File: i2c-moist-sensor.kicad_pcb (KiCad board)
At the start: 4 copper layers, 18 x 149 mm, 25 parts, among them IC1 ATTINY441-SSU, P1 CONN_02X03, X1 16MHz

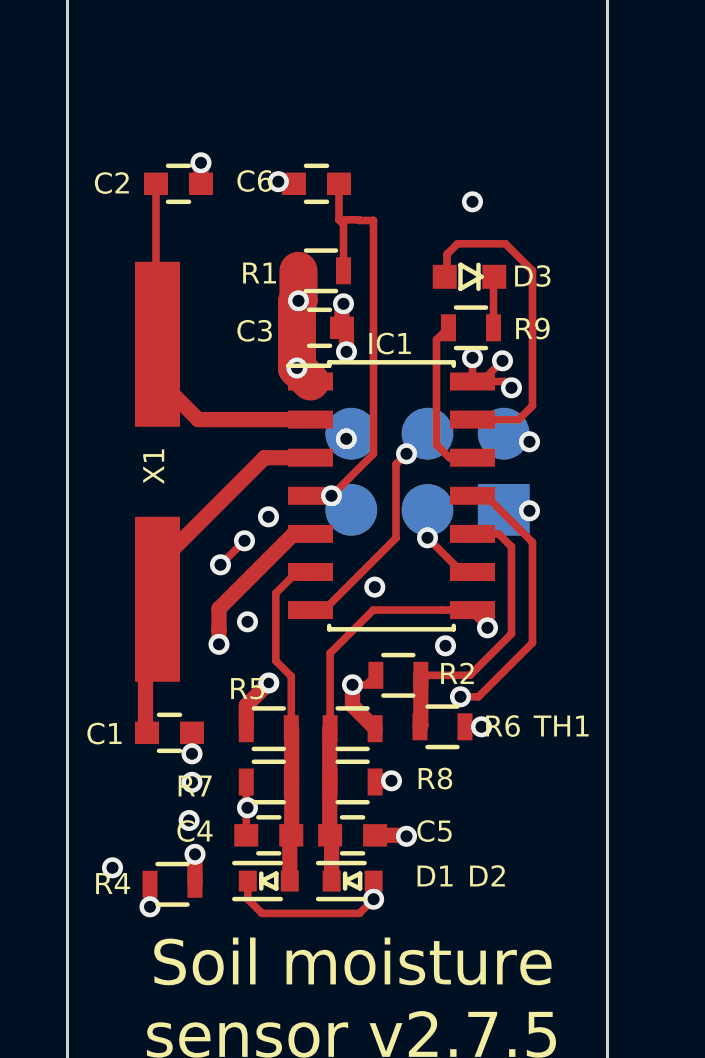
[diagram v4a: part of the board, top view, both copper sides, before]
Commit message: changed crystal to SMD 3225
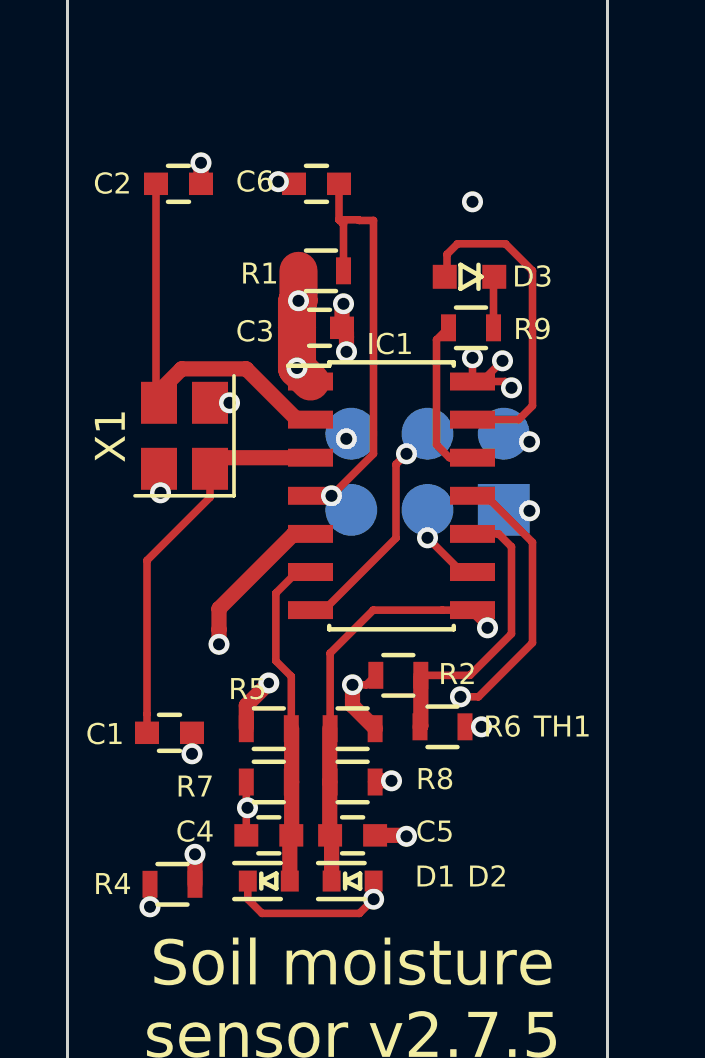
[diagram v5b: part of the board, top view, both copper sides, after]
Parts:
- X1: footprint Crystals:Crystal_HC49-SD_SMD -> Crystals:Crystal_SMD_3225-4pin_3.2x2.5mm
- moved X1 1.50 mm to (89.9, 41.8)
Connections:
- X1 pad 2: Net-(C2-Pad1) -> GND
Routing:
- net GND: track 57.8 -> 28.5 mm, vias 23 -> 16
- net Net-(C2-Pad1): track 12.9 -> 13.8 mm
- net Net-(C1-Pad1): track 12.3 -> 13.2 mm

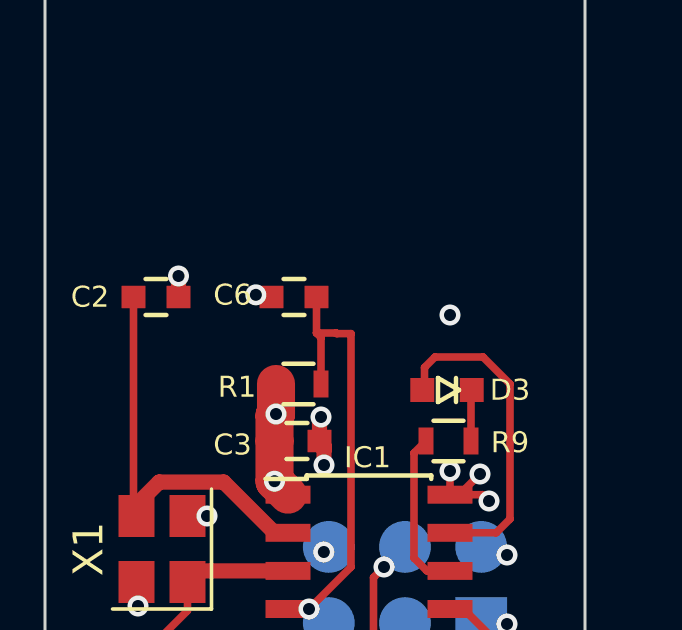
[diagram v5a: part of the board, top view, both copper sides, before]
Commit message: created and added 3D models, generated STEP file
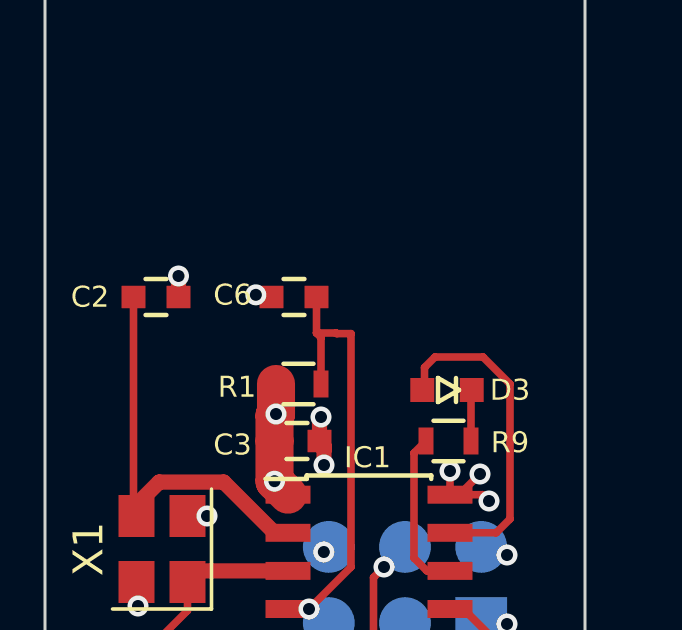
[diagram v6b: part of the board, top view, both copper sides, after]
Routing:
- net GND: track 28.5 -> 23.3 mm, vias 16 -> 15
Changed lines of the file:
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@@
-(kicad_pcb (version 20171130) (host pcbnew "(5.0.0-rc2-160-g7b73557)")
+(kicad_pcb (version 20171130) (host pcbnew "(6.0.0-rc1-dev-135-gb4df06c)")
   (general
     (thickness 1.6)
     (drawings 14)
-    (tracks 199)
+    (tracks 197)
     (zones 0)
     (modules 25)
@@
     (zone_45_only no)
     (trace_min 0.254)
-    (segment_width 0.2)
-    (edge_width 0.1)
     (via_size 0.7)
     (via_drill 0.4)
@@
     (uvia_min_size 0.508)
     (uvia_min_drill 0.127)
+    (edge_width 0.1)
+    (segment_width 0.2)
     (pcb_text_width 0.3)
     (pcb_text_size 0.7 0.7)
@@
       (drillshape 0)
       (scaleselection 1)
-      (outputdirectory gerbers-four-layers/))
+      (outputdirectory "gerbers-four-layers/"))
   )
   (net 0 "")
@@
     (pad 4 smd rect (at -1.1 -0.85 90) (size 1.4 1.2) (layers F.Cu F.Paste F.Mask)
       (net 2 GND))
-    (model ${KISYS3DMOD}/Crystals.3dshapes/Crystal_SMD_3225-4pin_3.2x2.5mm.wrl
-      (at (xyz 0 0 0))
-      (scale (xyz 1 1 1))
-      (rotate (xyz 0 0 0))
+    (model ${KIPRJMOD}/3d/CRY_SMD3225.STEP
+      (at (xyz 0 0 0))
+      (scale (xyz 1 1 1))
+      (rotate (xyz -90 0 0))
     )
   )
@@
   (segment (start 99.25 51.5) (end 99.8 51.5) (width 0.254) (layer F.Cu) (net 2))
   (via (at 99.8 51.5) (size 0.7) (drill 0.4) (layers F.Cu B.Cu) (net 2))
-  (segment (start 99.5 39.2) (end 99.5 34) (width 0.508) (layer In2.Cu) (net 2))
-  (via (at 99.5 34) (size 0.7) (drill 0.4) (layers F.Cu B.Cu) (net 2))
   (segment (start 91.96 55.118) (end 91.96 54.24) (width 0.254) (layer F.Cu) (net 2))
   (segment (start 91.96 54.24) (end 92 54.2) (width 0.254) (layer F.Cu) (net 2))

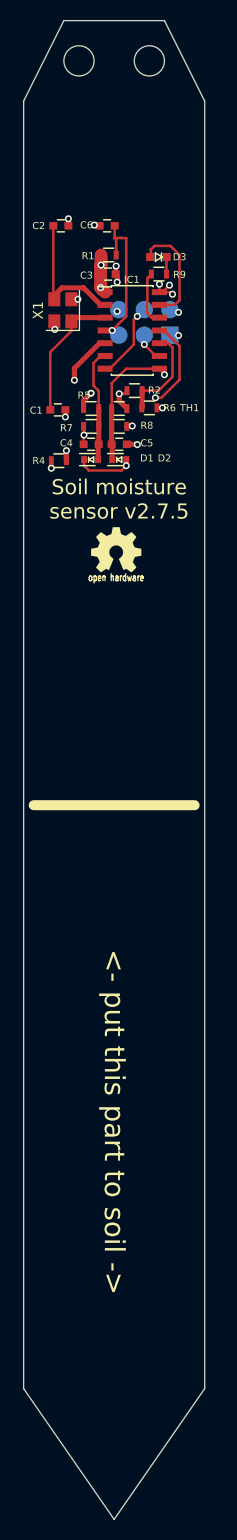
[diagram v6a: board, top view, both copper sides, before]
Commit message: Move stuff around, shorten traces to crystal, fix silkscreen, add cable connector pads, send files for manufacturing
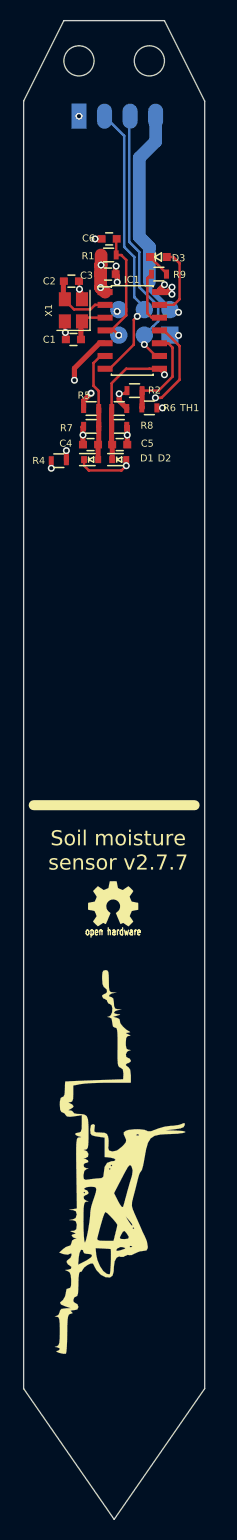
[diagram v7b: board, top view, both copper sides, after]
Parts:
- added P2: CONN_01X04, Pin_Headers:Pin_Header_Straight_1x04_Pitch2.54mm, B.Cu at (91.5, 22.5)
- G***: moved to B.Cu
- moved G*** 89.4 mm to (95.7, 126.4), turned to 270 degrees
- moved G*** 35.2 mm to (94.9, 100.8)
- moved C1 7.17 mm to (91.0, 44.7), turned to 180 degrees
- moved C2 5.60 mm to (90.8, 38.9)
- moved C6 1.32 mm to (94.5, 34.7)
- moved X1 1.05 mm to (91.0, 41.8)
- moved C4 0.07 mm to (92.7, 55.1)
- moved C5 0.06 mm to (95.5, 55.1)
- turned D3 to 90 degrees
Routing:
- net /SCK/SCL: track 3.35 -> 26.9 mm
- net VCC: track 13.9 -> 35.0 mm
- net /MOSI/SDA: track 7.78 -> 28.6 mm
- net Net-(C1-Pad1): track 13.2 -> 4.29 mm
- net Net-(C2-Pad1): track 13.8 -> 6.61 mm
- net Net-(D3-Pad1): track 10.8 -> 7.41 mm
- net /RESET: track 14.6 -> 13.3 mm
- net GND: track 23.3 -> 24.3 mm, vias 15 -> 13
- net Net-(D3-Pad2): track 1.72 -> 2.37 mm
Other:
- board text added: "GND SDA SCL VCC"
- board text added: "Soil moisture sensor v2.7.7"
- board text removed: "<- put this part to soil ->"
- board text removed: "Soil moisture sensor v2.7.5"

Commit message: Change shape of the board to accomodate narrower heatshrink, recover schematics from kicad version rescue hell
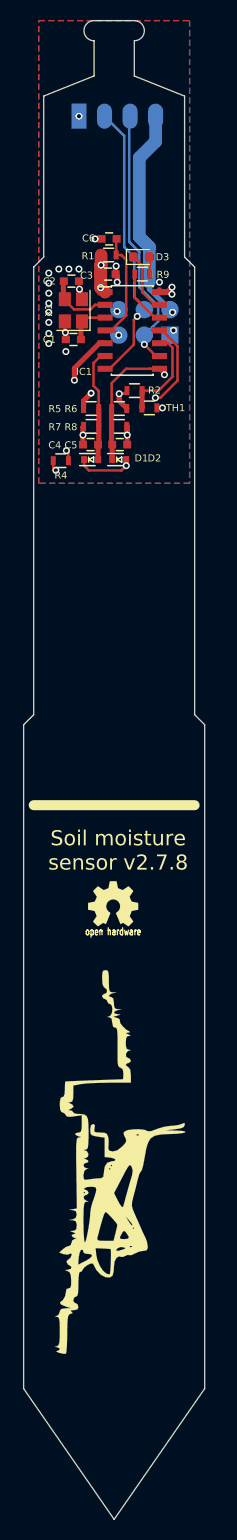
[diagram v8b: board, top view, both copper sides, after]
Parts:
- removed REF** (x2): MountingHole_3mm, Mounting_Holes:MountingHole_3mm
- D3: footprint LEDs:LED-0603 -> LED_SMD:LED_0603_1608Metric
- moved D3 1.70 mm to (97.7, 36.5), turned to 0 degrees
- moved R9 1.65 mm to (97.8, 38.2)
- moved R4 0.20 mm to (89.7, 56.8)
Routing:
- net Net-(D3-Pad1): track 7.41 -> 6.10 mm
- net VCC: track 35.0 -> 33.8 mm
- net GND: track 24.3 -> 23.6 mm, vias 13 -> 25
- net Net-(D3-Pad2): track 2.37 -> 1.73 mm
- added copper zone on B.Cu, net GND
- added copper zone on F.Cu, net GND
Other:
- outline, holes or cut-outs redrawn
- board text added: "Soil moisture sensor v2.7.8"
- board text removed: "Soil moisture sensor v2.7.7"
